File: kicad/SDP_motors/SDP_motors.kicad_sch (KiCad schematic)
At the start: 76 parts, among them J1 Conn_01x04, J10 MOTOR, J2 Conn_01x04, J3 Conn_01x04, J4 Conn_01x04, J5 Conn_01x04, J6 Conn_01x04, J7 Conn_01x02, J8 Conn_01x02, J9 Conn_01x02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

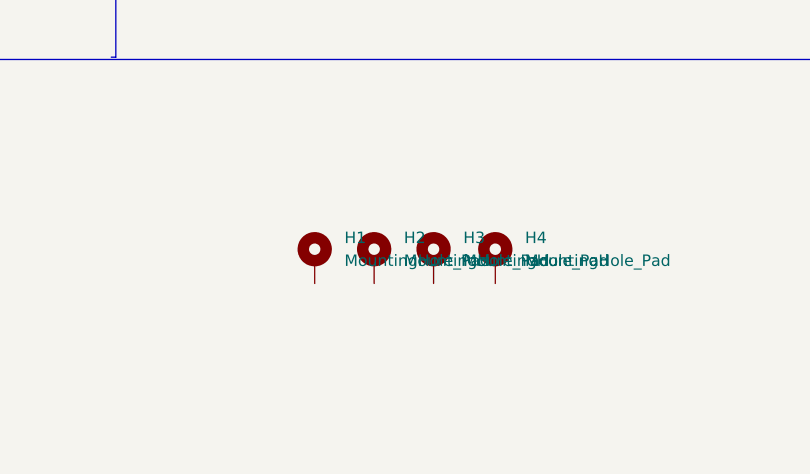
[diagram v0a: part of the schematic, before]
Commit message: Controller and motor PCB silkscreen and final layout
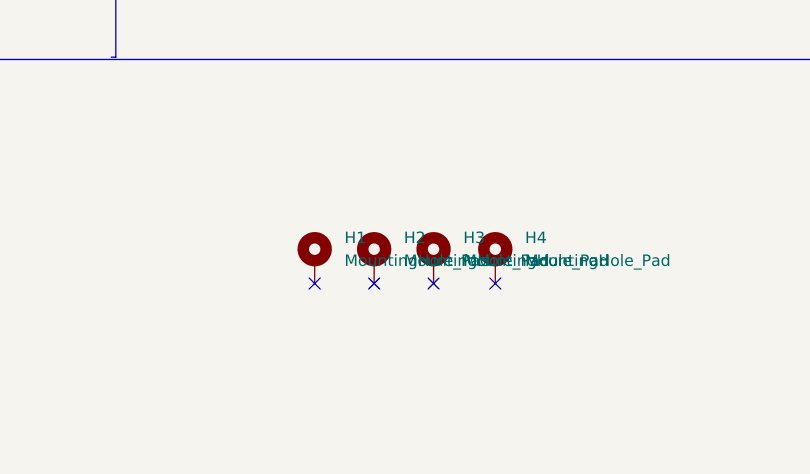
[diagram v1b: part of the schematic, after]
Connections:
- no-connect marks 0 -> 4
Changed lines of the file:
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@@
   (junction (at 229.87 60.452) (diameter 0) (color 0 0 0 0)
   )
+  (no_connect (at 325.882 190.754))
+  (no_connect (at 319.024 190.754))
+  (no_connect (at 312.42 190.754))
+  (no_connect (at 305.816 190.754))
   (wire (pts (xy 63.754 202.438) (xy 63.754 203.454))
     (stroke (width 0) (type default) (color 0 0 0 0))

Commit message: Final PCB layout changes
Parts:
- J7, J8, J9: footprint Connector_PinSocket_2.54mm:PinSocket_1x02_P2.54mm_Vertical -> TerminalBlock_Phoenix:TerminalBlock_Phoenix_PT-1,5-2-5.0-H_1x02_P5.00mm_Horizontal
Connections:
- net +12V: now also J7.1 (Pin_1), J8.1 (Pin_1), J9.1 (Pin_1); no longer J7.2 (Pin_2), J8.2 (Pin_2), J9.2 (Pin_2)
- net at D1.2 (A), Q1.2 (D): now also J7.2 (Pin_2); no longer J7.1 (Pin_1)
- net at D3.2 (A), Q3.2 (D): now also J9.2 (Pin_2); no longer J9.1 (Pin_1)
- net at D2.2 (A), Q2.2 (D): now also J8.2 (Pin_2); no longer J8.1 (Pin_1)
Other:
- moved on the sheet: J7, J8, J9
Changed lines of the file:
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@@
     (pin "1")
   )
-  (symbol (lib_id "Connector_Generic:Conn_01x02") (at 312.928 55.118 180) (unit 1)
-    (in_bom yes) (on_board yes) (fields_autoplaced)
-    (property "Reference" "J7" (id 0) (at 312.928 46.228 0))
-    (property "Value" "Conn_01x02" (id 1) (at 312.928 48.768 0))
-    (property "Footprint" "Connector_PinSocket_2.54mm:PinSocket_1x02_P2.54mm_Vertical" (id 2) (at 312.928 55.118 0)
-      (effects (font (size 1.27 1.27)) hide)
-    )
-    (property "Datasheet" "~" (id 3) (at 312.928 55.118 0)
+  (symbol (lib_id "Connector_Generic:Conn_01x02") (at 312.928 52.578 0) (mirror y) (unit 1)
+    (in_bom yes) (on_board yes) (fields_autoplaced)
+    (property "Reference" "J7" (id 0) (at 312.928 45.72 0))
+    (property "Value" "Conn_01x02" (id 1) (at 312.928 48.26 0))
+    (property "Footprint" "TerminalBlock_Phoenix:TerminalBlock_Phoenix_PT-1,5-2-5.0-H_1x02_P5.00mm_Horizontal" (id 2) (at 312.928 52.578 0)
+      (effects (font (size 1.27 1.27)) hide)
+    )
+    (property "Datasheet" "~" (id 3) (at 312.928 52.578 0)
       (effects (font (size 1.27 1.27)) hide)
     )
@@
     (pin "1")
   )
-  (symbol (lib_id "Connector_Generic:Conn_01x02") (at 313.944 116.586 180) (unit 1)
-    (in_bom yes) (on_board yes) (fields_autoplaced)
-    (property "Reference" "J8" (id 0) (at 313.944 107.696 0))
-    (property "Value" "Conn_01x02" (id 1) (at 313.944 110.236 0))
-    (property "Footprint" "Connector_PinSocket_2.54mm:PinSocket_1x02_P2.54mm_Vertical" (id 2) (at 313.944 116.586 0)
-      (effects (font (size 1.27 1.27)) hide)
-    )
-    (property "Datasheet" "~" (id 3) (at 313.944 116.586 0)
+  (symbol (lib_id "Connector_Generic:Conn_01x02") (at 313.944 114.046 0) (mirror y) (unit 1)
+    (in_bom yes) (on_board yes) (fields_autoplaced)
+    (property "Reference" "J8" (id 0) (at 313.944 107.95 0))
+    (property "Value" "Conn_01x02" (id 1) (at 313.944 110.49 0))
+    (property "Footprint" "TerminalBlock_Phoenix:TerminalBlock_Phoenix_PT-1,5-2-5.0-H_1x02_P5.00mm_Horizontal" (id 2) (at 313.944 114.046 0)
+      (effects (font (size 1.27 1.27)) hide)
+    )
+    (property "Datasheet" "~" (id 3) (at 313.944 114.046 0)
       (effects (font (size 1.27 1.27)) hide)
     )
@@
     (pin "3")
   )
-  (symbol (lib_id "Connector_Generic:Conn_01x02") (at 367.792 55.118 180) (unit 1)
-    (in_bom yes) (on_board yes) (fields_autoplaced)
-    (property "Reference" "J9" (id 0) (at 367.792 46.228 0))
-    (property "Value" "Conn_01x02" (id 1) (at 367.792 48.768 0))
-    (property "Footprint" "Connector_PinSocket_2.54mm:PinSocket_1x02_P2.54mm_Vertical" (id 2) (at 367.792 55.118 0)
-      (effects (font (size 1.27 1.27)) hide)
-    )
-    (property "Datasheet" "~" (id 3) (at 367.792 55.118 0)
+  (symbol (lib_id "Connector_Generic:Conn_01x02") (at 367.792 52.578 0) (mirror y) (unit 1)
+    (in_bom yes) (on_board yes) (fields_autoplaced)
+    (property "Reference" "J9" (id 0) (at 367.792 45.72 0))
+    (property "Value" "Conn_01x02" (id 1) (at 367.792 48.26 0))
+    (property "Footprint" "TerminalBlock_Phoenix:TerminalBlock_Phoenix_PT-1,5-2-5.0-H_1x02_P5.00mm_Horizontal" (id 2) (at 367.792 52.578 0)
+      (effects (font (size 1.27 1.27)) hide)
+    )
+    (property "Datasheet" "~" (id 3) (at 367.792 52.578 0)
       (effects (font (size 1.27 1.27)) hide)
     )
@@
     )
     (path "/0695aec6-d2b7-4658-bf5f-6dd0faecc8fa"
-      (reference "J7") (unit 1) (value "Conn_01x02") (footprint "Connector_PinSocket_2.54mm:PinSocket_1x02_P2.54mm_Vertical")
+      (reference "J7") (unit 1) (value "Conn_01x02") (footprint "TerminalBlock_Phoenix:TerminalBlock_Phoenix_PT-1,5-2-5.0-H_1x02_P5.00mm_Horizontal")
     )
     (path "/53f2ddc8-594c-4867-8cf0-5374c2eb5197"
-      (reference "J8") (unit 1) (value "Conn_01x02") (footprint "Connector_PinSocket_2.54mm:PinSocket_1x02_P2.54mm_Vertical")
+      (reference "J8") (unit 1) (value "Conn_01x02") (footprint "TerminalBlock_Phoenix:TerminalBlock_Phoenix_PT-1,5-2-5.0-H_1x02_P5.00mm_Horizontal")
     )
     (path "/af719119-80a2-4e54-ad0a-db748541c24d"
-      (reference "J9") (unit 1) (value "Conn_01x02") (footprint "Connector_PinSocket_2.54mm:PinSocket_1x02_P2.54mm_Vertical")
+      (reference "J9") (unit 1) (value "Conn_01x02") (footprint "TerminalBlock_Phoenix:TerminalBlock_Phoenix_PT-1,5-2-5.0-H_1x02_P5.00mm_Horizontal")
     )
     (path "/fa3996ea-58a5-40c8-b8c5-862af4766ad0"
